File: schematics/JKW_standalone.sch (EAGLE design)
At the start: 217 parts, among them IC1 4093D, IC2 AT-MEGA-8L, IC4 ATMEGA2560-16AU, Q1 BSS84, Q10 BSS84, Q11 BSS84, Q2 BSS84, Q3 BSS84, Q4 BSS84, Q5 BSS84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

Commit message: ATm8 update: increased number of waiting steps to start 'go_back'
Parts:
- added PE: 100nF, RCLDT:C0805
- R_REED_DOWN: value 5k / n.b. (Reed) -> 5k / n.b. (Reed / 5V Honda Signal)
- R_REED_UP: value n.b. / 5k (Reed) -> n.b.(Honda Signal) / 5k (Reed)
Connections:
- net GND: now also PE.1
- net VDD: now also PE.2
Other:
- moved on the sheet: 12V_F1, 3.3V_SUPPLY, 5V_F, 5V_SUPPLY, C11, C18, C39, CP1, CP2, CP3, CP4, D12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

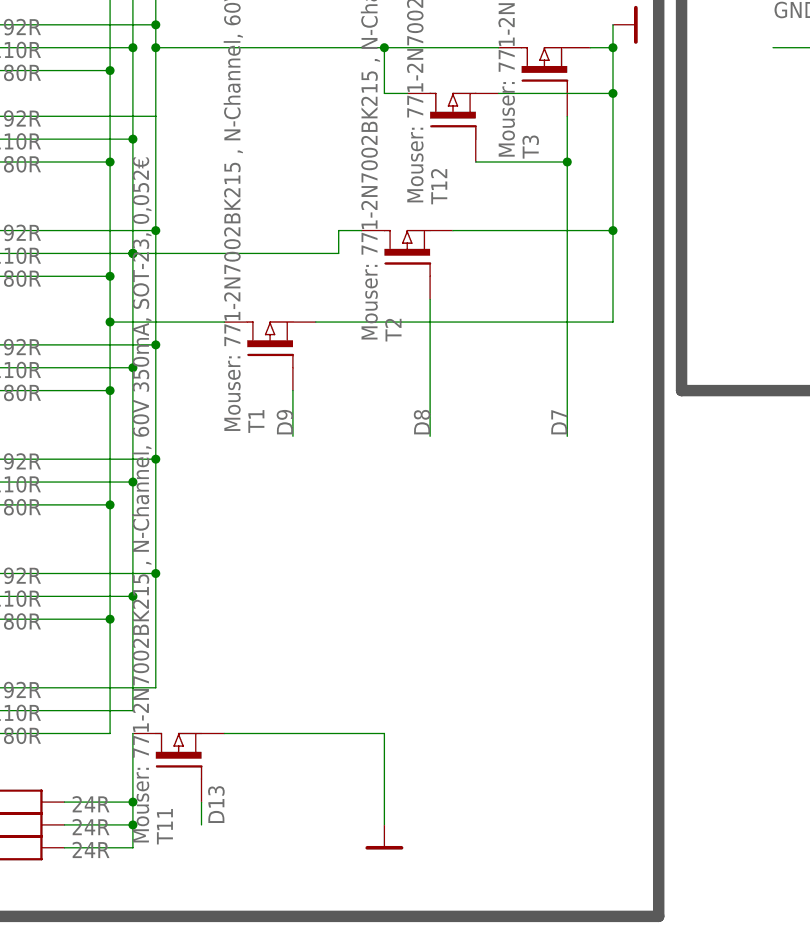
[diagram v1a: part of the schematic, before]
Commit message: added pull down for dimm transistors
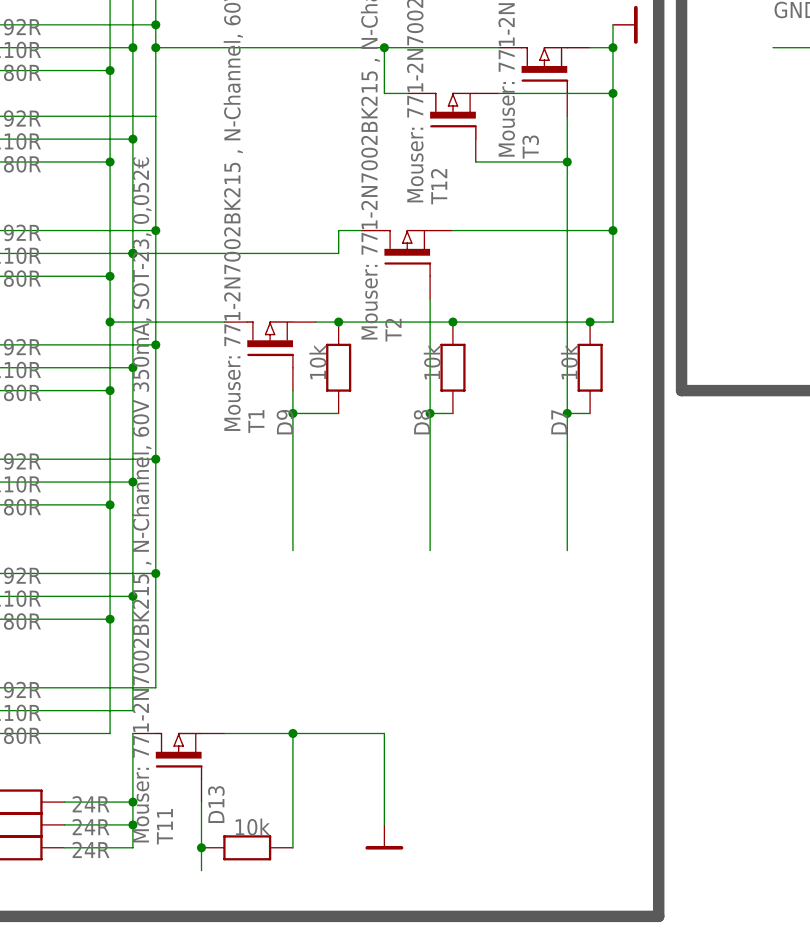
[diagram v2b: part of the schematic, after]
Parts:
- added R_B_LED_12, R_B_LED_13, R_B_LED_14, R_B_LED_15: 10k, RCLDT:R0805
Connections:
- net D13: now also R_B_LED_12.1
- net D7: now also R_B_LED_15.1
- net D8: now also R_B_LED_14.1
- net D9: now also R_B_LED_13.1
- net GND: now also R_B_LED_12.2, R_B_LED_13.2, R_B_LED_14.2, R_B_LED_15.2
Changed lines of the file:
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@@
 <?xml version="1.0" encoding="utf-8"?>
 <!DOCTYPE eagle SYSTEM "eagle.dtd">
-<eagle version="6.2">
+<eagle version="6.1">
 <drawing>
 <settings>
@@
 <part name="U$20" library="SUPPLY" deviceset="GND" device=""/>
 <part name="PE" library="RCLDT" deviceset="C" device="0805" value="100nF"/>
+<part name="R_B_LED_12" library="RCLDT" deviceset="R" device="0805" value="10k"/>
+<part name="R_B_LED_13" library="RCLDT" deviceset="R" device="0805" value="10k"/>
+<part name="R_B_LED_14" library="RCLDT" deviceset="R" device="0805" value="10k"/>
+<part name="R_B_LED_15" library="RCLDT" deviceset="R" device="0805" value="10k"/>
 </parts>
 <sheets>
@@
 <attribute name="VALUE" x="-93.98" y="2.54" size="1.778" layer="96" rot="R270"/>
 </instance>
+<instance part="R_B_LED_12" gate="G$1" x="68.58" y="-81.28" smashed="yes">
+<attribute name="VALUE" x="71.12" y="-78.105" size="1.778" layer="96" rot="R180"/>
+</instance>
+<instance part="R_B_LED_13" gate="G$1" x="78.74" y="-27.94" smashed="yes" rot="R90">
+<attribute name="VALUE" x="75.565" y="-25.4" size="1.778" layer="96" rot="R270"/>
+</instance>
+<instance part="R_B_LED_14" gate="G$1" x="91.44" y="-27.94" smashed="yes" rot="R90">
+<attribute name="VALUE" x="88.265" y="-25.4" size="1.778" layer="96" rot="R270"/>
+</instance>
+<instance part="R_B_LED_15" gate="G$1" x="106.68" y="-27.94" smashed="yes" rot="R90">
+<attribute name="VALUE" x="103.505" y="-25.4" size="1.778" layer="96" rot="R270"/>
+</instance>
 </instances>
 <busses>
@@
 <wire x1="109.22" y1="-12.7" x2="91.44" y2="-12.7" width="0.1524" layer="91"/>
 <wire x1="109.22" y1="-12.7" x2="109.22" y2="-22.86" width="0.1524" layer="91"/>
-<wire x1="109.22" y1="-22.86" x2="76.2" y2="-22.86" width="0.1524" layer="91"/>
+<wire x1="109.22" y1="-22.86" x2="106.68" y2="-22.86" width="0.1524" layer="91"/>
 <junction x="109.22" y="-12.7"/>
 <junction x="109.22" y="7.62"/>
@@
 <pinref part="T1" gate="G$1" pin="S"/>
 <pinref part="T12" gate="G$1" pin="S"/>
+<wire x1="106.68" y1="-22.86" x2="91.44" y2="-22.86" width="0.1524" layer="91"/>
+<wire x1="91.44" y1="-22.86" x2="78.74" y2="-22.86" width="0.1524" layer="91"/>
+<wire x1="78.74" y1="-22.86" x2="76.2" y2="-22.86" width="0.1524" layer="91"/>
 <wire x1="96.52" y1="2.54" x2="109.22" y2="2.54" width="0.1524" layer="91"/>
 <junction x="109.22" y="2.54"/>
+<pinref part="R_B_LED_13" gate="G$1" pin="2"/>
+<junction x="78.74" y="-22.86"/>
+<pinref part="R_B_LED_14" gate="G$1" pin="2"/>
+<junction x="91.44" y="-22.86"/>
+<pinref part="R_B_LED_15" gate="G$1" pin="2"/>
+<junction x="106.68" y="-22.86"/>
 </segment>
 <segment>
@@
 <pinref part="T11" gate="G$1" pin="S"/>
 <pinref part="U$17" gate="G$1" pin="GND"/>
-<wire x1="66.04" y1="-68.58" x2="83.82" y2="-68.58" width="0.1524" layer="91"/>
+<wire x1="66.04" y1="-68.58" x2="73.66" y2="-68.58" width="0.1524" layer="91"/>
+<wire x1="73.66" y1="-68.58" x2="83.82" y2="-68.58" width="0.1524" layer="91"/>
 <wire x1="83.82" y1="-68.58" x2="83.82" y2="-78.74" width="0.1524" layer="91"/>
+<pinref part="R_B_LED_12" gate="G$1" pin="2"/>
+<wire x1="73.66" y1="-81.28" x2="73.66" y2="-68.58" width="0.1524" layer="91"/>
+<junction x="73.66" y="-68.58"/>
 </segment>
 <segment>
@@
 <pinref part="T3" gate="G$1" pin="G"/>
 <pinref part="T12" gate="G$1" pin="G"/>
-<wire x1="104.14" y1="-5.08" x2="104.14" y2="-35.56" width="0.1524" layer="91"/>
+<wire x1="104.14" y1="-5.08" x2="104.14" y2="-33.02" width="0.1524" layer="91"/>
+<wire x1="104.14" y1="-33.02" x2="104.14" y2="-48.26" width="0.1524" layer="91"/>
 <wire x1="93.98" y1="-5.08" x2="104.14" y2="-5.08" width="0.1524" layer="91"/>
 <junction x="104.14" y="-5.08"/>
+<pinref part="R_B_LED_15" gate="G$1" pin="1"/>
+<wire x1="106.68" y1="-33.02" x2="104.14" y2="-33.02" width="0.1524" layer="91"/>
+<junction x="104.14" y="-33.02"/>
 </segment>
 </net>
@@
 </segment>
 <segment>
-<wire x1="88.9" y1="-20.32" x2="88.9" y2="-35.56" width="0.1524" layer="91"/>
+<wire x1="88.9" y1="-20.32" x2="88.9" y2="-33.02" width="0.1524" layer="91"/>
 <label x="88.9" y="-35.56" size="1.778" layer="95" rot="R90"/>
 <pinref part="T2" gate="G$1" pin="G"/>
+<pinref part="R_B_LED_14" gate="G$1" pin="1"/>
+<wire x1="88.9" y1="-33.02" x2="88.9" y2="-48.26" width="0.1524" layer="91"/>
+<wire x1="91.44" y1="-33.02" x2="88.9" y2="-33.02" width="0.1524" layer="91"/>
+<junction x="88.9" y="-33.02"/>
 </segment>
 </net>
@@
 </segment>
 <segment>
-<wire x1="73.66" y1="-30.48" x2="73.66" y2="-35.56" width="0.1524" layer="91"/>
+<wire x1="73.66" y1="-30.48" x2="73.66" y2="-33.02" width="0.1524" layer="91"/>
 <label x="73.66" y="-35.56" size="1.778" layer="95" rot="R90"/>
 <pinref part="T1" gate="G$1" pin="G"/>
+<pinref part="R_B_LED_13" gate="G$1" pin="1"/>
+<wire x1="73.66" y1="-33.02" x2="73.66" y2="-48.26" width="0.1524" layer="91"/>
+<wire x1="78.74" y1="-33.02" x2="73.66" y2="-33.02" width="0.1524" layer="91"/>
+<junction x="73.66" y="-33.02"/>
 </segment>
 </net>
@@
 <segment>
 <pinref part="T11" gate="G$1" pin="G"/>
-<wire x1="63.5" y1="-76.2" x2="63.5" y2="-78.74" width="0.1524" layer="91"/>
+<wire x1="63.5" y1="-76.2" x2="63.5" y2="-81.28" width="0.1524" layer="91"/>
 <label x="66.04" y="-78.74" size="1.778" layer="95" rot="R90"/>
-</segment>
-</net>
+<pinref part="R_B_LED_12" gate="G$1" pin="1"/>
+<wire x1="63.5" y1="-81.28" x2="63.5" y2="-83.82" width="0.1524" layer="91"/>
+<junction x="63.5" y="-81.28"/>
+</segment>
+</net>

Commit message: improved overvoltage schematic
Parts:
- removed D12: 20V-Zdiode, diode:ZENER-DIODESOD80C
- added D11: 20V-Zdiode, diode:ZENER-DIODESOT23
- added R_HB5: 600R, RCLDT:R0805
- added R_OIL_OV, R_OIL_OV1: 1k, RCLDT:R0805
- added R_R_LED_12: 220R, RCLDT:R0805
- C35: value 22p -> 100nF
- C5, C7: value 100nF -> 22pF
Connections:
- new net N$109: D11.A, R_R_LED_12.2
- new net N$110: R_HB5.1, SPEEDOSTECKER.NEUTRAL_GEAR
- new net N$111: R_OIL_OV1.1, R_WATER_UP.2, SPEEDOSTECKER.WATER_TEMP
- new net N999: R_OIL_OV.1, R_OIL_UP.1, SPEEDOSTECKER.OIL_TEMP
- net A0: now also R_OIL_OV1.2; no longer R_WATER_UP.2, SPEEDOSTECKER.WATER_TEMP
- net A1: now also R_OIL_OV.2; no longer R_OIL_UP.1, SPEEDOSTECKER.OIL_TEMP
- net GND: now also R_R_LED_12.1; no longer D12.A
- net N$1: now also D11.C; no longer D12.C
- net NG_IN: now also R_HB5.2; no longer SPEEDOSTECKER.NEUTRAL_GEAR
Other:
- moved on the sheet: D10, D18, D20, D22, D3, D_P_EX_D2, R_E2_0, R_E2_2, R_HB1, R_OIL_UP, R_WATER_UP

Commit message: Added correct overvoltage z-diode
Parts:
- removed R_B_LED_0, R_G_LED_0: 24R, RCLDT:R0805
- removed U$1: CLP6B-WKW-CD0E0233, Kolja:CLP6B-WKW-CD0E0233
- added U$22: CLM4B-RKW-CWAXBAA3, Kolja:CLM4B-RKW-CWAXBAA3
- R_R_LED_0: value 24R -> 52R
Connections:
- removed net N$63: R_G_LED_0.1, U$1.P$1
- removed net N$65: R_B_LED_0.1, U$1.P$2
- net N$16: now also U$22.CATHODE; no longer U$1.CATHODE
- net N$71: no longer R_B_LED_0.2, R_G_LED_0.2
- net VDD: now also U$22.ANODE; no longer U$1.ANODE
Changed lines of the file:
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@@
 <?xml version="1.0" encoding="utf-8"?>
 <!DOCTYPE eagle SYSTEM "eagle.dtd">
-<eagle version="6.2">
+<eagle version="6.1">
 <drawing>
 <settings>
@@
 <part name="R_G_LED_1" library="RCLDT" deviceset="R" device="0805" value="110R"/>
 <part name="R_B_LED_1" library="RCLDT" deviceset="R" device="0805" value="80R"/>
-<part name="R_R_LED_0" library="RCLDT" deviceset="R" device="0805" value="24R"/>
-<part name="R_G_LED_0" library="RCLDT" deviceset="R" device="0805" value="24R"/>
-<part name="R_B_LED_0" library="RCLDT" deviceset="R" device="0805" value="24R"/>
+<part name="R_R_LED_0" library="RCLDT" deviceset="R" device="0805" value="52R"/>
 <part name="T1" library="RCLDT" deviceset="T-P-FET" device="BSS139" value="Mouser: 771-2N7002BK215 , N-Channel, 60V 350mA, SOT-23, 0,052€"/>
 <part name="T2" library="RCLDT" deviceset="T-P-FET" device="BSS139" value="Mouser: 771-2N7002BK215 , N-Channel, 60V 350mA, SOT-23, 0,052€"/>
@@
 <part name="R_SD_PWR_UP" library="RCLDT" deviceset="R" device="0805" value="10k"/>
 <part name="R_RES_UP" library="RCLDT" deviceset="R" device="0805" value="10k"/>
-<part name="U$1" library="Kolja" deviceset="CLP6B-WKW-CD0E0233" device=""/>
 <part name="U$3" library="Kolja" deviceset="CLM4B-BKW-CTBVA363" device=""/>
 <part name="U$11" library="Kolja" deviceset="CLM4B-RKW-CWAXBAA3" device=""/>
@@
 <part name="R_HB5" library="RCLDT" deviceset="R" device="0805" value="600R"/>
 <part name="R_OIL_OV1" library="RCLDT" deviceset="R" device="0805" value="1k"/>
+<part name="U$22" library="Kolja" deviceset="CLM4B-RKW-CWAXBAA3" device=""/>
 </parts>
 <sheets>
@@
 <attribute name="VALUE" x="53.34" y="-75.565" size="1.778" layer="96" rot="R180"/>
 </instance>
-<instance part="R_G_LED_0" gate="G$1" x="43.18" y="-78.74" smashed="yes">
-<attribute name="VALUE" x="53.34" y="-78.105" size="1.778" layer="96" rot="R180"/>
-</instance>
-<instance part="R_B_LED_0" gate="G$1" x="43.18" y="-81.28" smashed="yes">
-<attribute name="VALUE" x="53.34" y="-80.645" size="1.778" layer="96" rot="R180"/>
-</instance>
 <instance part="T1" gate="G$1" x="71.12" y="-25.4" rot="MR90"/>
 <instance part="T2" gate="G$1" x="86.36" y="-15.24" rot="MR90"/>
@@
 <instance part="R_SD_PWR_UP" gate="G$1" x="-35.56" y="119.38" rot="MR90"/>
 <instance part="R_RES_UP" gate="G$1" x="-294.64" y="208.28" rot="MR90"/>
-<instance part="U$1" gate="G$1" x="15.24" y="-76.2"/>
 <instance part="U$3" gate="G$1" x="383.54" y="2.54" rot="R90"/>
 <instance part="U$11" gate="G$1" x="370.84" y="2.54" rot="R90"/>
@@
 <instance part="R_HB5" gate="G$1" x="91.44" y="187.96" rot="R180"/>
 <instance part="R_OIL_OV1" gate="G$1" x="58.42" y="139.7" rot="R180"/>
+<instance part="U$22" gate="G$1" x="25.4" y="-76.2"/>
 </instances>
 <busses>
@@
 <segment>
 <pinref part="SUPPLY15" gate="G$1" pin="VDD"/>
-<wire x1="7.62" y1="-76.2" x2="-2.54" y2="-76.2" width="0.1524" layer="91"/>
-<pinref part="U$1" gate="G$1" pin="ANODE"/>
+<wire x1="20.32" y1="-76.2" x2="-2.54" y2="-76.2" width="0.1524" layer="91"/>
+<pinref part="U$22" gate="G$1" pin="ANODE"/>
 </segment>
 <segment>
@@
 <pinref part="T11" gate="G$1" pin="G"/>
 <wire x1="63.5" y1="-76.2" x2="63.5" y2="-81.28" width="0.1524" layer="91"/>
-<label x="66.04" y="-78.74" size="1.778" layer="95" rot="R90"/>
 <pinref part="R_B_LED_12" gate="G$1" pin="1"/>
 <wire x1="63.5" y1="-81.28" x2="63.5" y2="-83.82" width="0.1524" layer="91"/>
 <junction x="63.5" y="-81.28"/>
+<label x="60.96" y="-86.36" size="1.778" layer="95"/>
 </segment>
 </net>
@@
 </segment>
 </net>
-<net name="N$65" class="0">
-<segment>
-<wire x1="38.1" y1="-81.28" x2="20.32" y2="-81.28" width="0.1524" layer="91"/>
-<pinref part="R_B_LED_0" gate="G$1" pin="1"/>
-<pinref part="U$1" gate="G$1" pin="P$2"/>
-</segment>
-</net>
 <net name="N$24" class="0">
 <segment>
@@
 <net name="N$71" class="0">
 <segment>
-<pinref part="R_B_LED_0" gate="G$1" pin="2"/>
 <pinref part="T11" gate="G$1" pin="D"/>
-<wire x1="48.26" y1="-81.28" x2="55.88" y2="-81.28" width="0.1524" layer="91"/>
-<wire x1="55.88" y1="-81.28" x2="55.88" y2="-78.74" width="0.1524" layer="91"/>
-<pinref part="R_G_LED_0" gate="G$1" pin="2"/>
-<wire x1="55.88" y1="-78.74" x2="55.88" y2="-76.2" width="0.1524" layer="91"/>
 <wire x1="55.88" y1="-76.2" x2="55.88" y2="-68.58" width="0.1524" layer="91"/>
-<wire x1="48.26" y1="-78.74" x2="55.88" y2="-78.74" width="0.1524" layer="91"/>
 <pinref part="R_R_LED_0" gate="G$1" pin="2"/>
 <wire x1="48.26" y1="-76.2" x2="55.88" y2="-76.2" width="0.1524" layer="91"/>
-<junction x="55.88" y="-78.74"/>
-<junction x="55.88" y="-76.2"/>
-</segment>
-</net>
-<net name="N$16" class="0">
-<segment>
-<pinref part="R_R_LED_0" gate="G$1" pin="1"/>
-<pinref part="U$1" gate="G$1" pin="CATHODE"/>
-<wire x1="20.32" y1="-76.2" x2="38.1" y2="-76.2" width="0.1524" layer="91"/>
-</segment>
-</net>
-<net name="N$63" class="0">
-<segment>
-<wire x1="20.32" y1="-78.74" x2="38.1" y2="-78.74" width="0.1524" layer="91"/>
-<pinref part="R_G_LED_0" gate="G$1" pin="1"/>
-<pinref part="U$1" gate="G$1" pin="P$1"/>
 </segment>
 </net>
@@
 </segment>
 </net>
+<net name="N$16" class="0">
+<segment>
+<pinref part="R_R_LED_0" gate="G$1" pin="1"/>
+<wire x1="27.94" y1="-76.2" x2="28.448" y2="-76.2" width="0.1524" layer="91"/>
+<pinref part="U$22" gate="G$1" pin="CATHODE"/>
+<wire x1="28.448" y1="-76.2" x2="38.1" y2="-76.2" width="0.1524" layer="91"/>
+<junction x="28.448" y="-76.2"/>
+</segment>
+</net>

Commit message: added reset from ATM328 to 2560
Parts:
- added R_L3: 1k, RCLDT:R0805
- IC2: value AT-MEGA-8L -> AT-MEGA-328P-AU
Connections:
- net RESETAVR_AT8: now also IC4.(ICP1)PD4, R_L3.2
- net VDD: now also R_L3.1
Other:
- note added: "ATmega328P-AU"
- note removed: "ATmega8"
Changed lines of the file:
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@@
 <?xml version="1.0" encoding="utf-8"?>
 <!DOCTYPE eagle SYSTEM "eagle.dtd">
-<eagle version="6.1">
+<eagle version="6.2">
 <drawing>
 <settings>
@@
 <part name="U$161" library="SUPPLY" deviceset="GND" device=""/>
 <part name="GND4" library="SparkFun" deviceset="GND" device=""/>
-<part name="IC2" library="µP´s+Pic´s" deviceset="AT-MEGA-8" device="" value="AT-MEGA-8L"/>
+<part name="IC2" library="µP´s+Pic´s" deviceset="AT-MEGA-8" device="" value="AT-MEGA-328P-AU"/>
 <part name="AT8_REF" library="RCLDT" deviceset="R" device="0805" value="10R"/>
 <part name="U$5" library="SUPPLY" deviceset="GND" device=""/>
@@
 <part name="R_OIL_OV1" library="RCLDT" deviceset="R" device="0805" value="1k"/>
 <part name="U$22" library="Kolja" deviceset="CLM4B-RKW-CWAXBAA3" device=""/>
+<part name="R_L3" library="RCLDT" deviceset="R" device="0805" value="1k"/>
+<part name="SUPPLY22" library="supply2" deviceset="VDD" device=""/>
 </parts>
 <sheets>
@@
 <text x="-19.812" y="165.608" size="1.778" layer="91">ARD_TX</text>
 <text x="228.28" y="246.38" size="3.81" layer="95">i2c_temp</text>
-<text x="-220.98" y="66.04" size="5.08" layer="95">ATmega8</text>
+<text x="-220.98" y="66.04" size="5.08" layer="95">ATmega328P-AU</text>
 <text x="340.36" y="55.88" size="3.81" layer="95">Lichtlein &amp; Blinker</text>
 <text x="-7.62" y="53.34" size="3.81" layer="95">Instrumenten Beleuchtung</text>
@@
 <instance part="R_OIL_OV1" gate="G$1" x="58.42" y="139.7" rot="R180"/>
 <instance part="U$22" gate="G$1" x="25.4" y="-76.2"/>
+<instance part="R_L3" gate="G$1" x="-142.24" y="53.34" smashed="yes">
+<attribute name="VALUE" x="-132.08" y="53.975" size="1.778" layer="96" rot="R180"/>
+</instance>
+<instance part="SUPPLY22" gate="G$1" x="-149.86" y="60.96"/>
 </instances>
 <busses>
@@
 <junction x="-96.52" y="-5.08"/>
 </segment>
+<segment>
+<pinref part="R_L3" gate="G$1" pin="1"/>
+<pinref part="SUPPLY22" gate="G$1" pin="VDD"/>
+<wire x1="-147.32" y1="53.34" x2="-149.86" y2="53.34" width="0.1524" layer="91"/>
+<wire x1="-149.86" y1="53.34" x2="-149.86" y2="58.42" width="0.1524" layer="91"/>
+</segment>
 </net>
 <net name="CONNECT" class="0">
@@
 </segment>
 <segment>
-<wire x1="-134.62" y1="43.18" x2="-134.62" y2="71.12" width="0.1524" layer="91"/>
+<wire x1="-134.62" y1="43.18" x2="-134.62" y2="53.34" width="0.1524" layer="91"/>
 <label x="-134.3152" y="68.6816" size="1.778" layer="95" rot="R270"/>
 <pinref part="JP2" gate="A" pin="2"/>
+<pinref part="R_L3" gate="G$1" pin="2"/>
+<wire x1="-134.62" y1="53.34" x2="-134.62" y2="71.12" width="0.1524" layer="91"/>
+<wire x1="-137.16" y1="53.34" x2="-134.62" y2="53.34" width="0.1524" layer="91"/>
+<junction x="-134.62" y="53.34"/>
+</segment>
+<segment>
+<pinref part="IC4" gate="1" pin="(ICP1)PD4"/>
+<wire x1="-185.42" y1="162.56" x2="-170.18" y2="162.56" width="0.1524" layer="91"/>
+<label x="-182.88" y="162.56" size="1.778" layer="95"/>
 </segment>
 </net>

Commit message: Moved LED's to port expander
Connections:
- new net PE_A3: T9.G, U$19.A3
- new net PE_A4: T7.G, U$19.A4
- new net PE_A5: T6.G, U$19.A5
- new net PE_A6: T10.G, U$19.A6
- new net PE_A7: T8.G, U$19.A7
- net D42: no longer T7.G
- net D43: no longer T6.G
- net D44: no longer T10.G
- net D45: no longer T9.G
- net D46: no longer T8.G
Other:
- moved on the sheet: 12V_F1, 3.3V_SUPPLY, 5V_F, 5V_SUPPLY, C11, C18, C39, CP1, CP2, CP3, CP4, D11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

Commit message: changed controller
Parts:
- removed IC2: AT-MEGA-328P-AU, µP´s+Pic´s:AT-MEGA-8
- added U$1: ATMEGA328P-AU, Kolja:ATMEGA328P-AU
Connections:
- net A2: now also U$1.(PCINT20/XCK/T0)PD4; no longer IC2.T0/PD4
- net ARD_RES_OUT: now also U$1.(ADC5/PCINT13/SCL)PC5; no longer IC2.ADC5/PC5
- net CONNECT: now also U$1.(INT0/PCINT18)PD2; no longer IC2.INT0/PD2
- net D6: now also U$1.(PCINT19/OC2B/INT1)PD3; no longer IC2.INT1/PD3
- net GND: now also U$1.GND, U$1.GND@1, U$1.GND@2; no longer IC2.AGND, IC2.GND, IC2.GND@1
- net M1: now also U$1.(ADC0/PCINT8)PC0; no longer IC2.ADC0/PC0
- net M2: now also U$1.(ADC1/PCINT9)PC1; no longer IC2.ADC1/PC1
- net M3: now also U$1.(ADC2/PCINT10)PC2; no longer IC2.ADC2/PC2
- net M4: now also U$1.(ADC3/PCINT11)PC3; no longer IC2.ADC3/PC3
- net MISO_AT8: now also U$1.(PCINT4/MISO)PB4; no longer IC2.MISO/PB4
- net MOSI_AT8: now also U$1.(PCINT3/OC2A/MOSI)PB3; no longer IC2.MOSI/PB3
- net N$14: now also U$1.(PCINT23/AIN1)PD7; no longer IC2.AIN1/PD7
- net N$18: now also U$1.(PCINT22/OC0A/AIN0)PD6; no longer IC2.AIN0/PD6
- net N$20: now also U$1.(PCINT21/OC0B/T1)PD5; no longer IC2.T1/PD5
- net N$3: now also U$1.AREF, U$1.AVCC; no longer IC2.AREF, IC2.AVCC
- net RESETAVR_AT8: no longer IC2.RESET
- net RX3: now also U$1.(TXD/PCINT17)PD1; no longer IC2.TXD/PD1
- net SCK_AT8: now also U$1.(PCINT5/SCK)PB5; no longer IC2.SCK/PB5
- net TX3: now also U$1.(RXD/PCINT16)PD0; no longer IC2.RXD/PD0
- net V_AT8_BUFFERED: now also U$1.VCC@1, U$1.VCC@2; no longer IC2.VDD, IC2.VDD@1
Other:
- moved on the sheet: AT8_REF, C1, C2, C3, C_EMERGENCY, D9

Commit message: Moved AT in place
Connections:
- net RESETAVR_AT8: now also U$1.(!RESET!/PCINT14)PC6
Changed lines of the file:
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@@
 <?xml version="1.0" encoding="utf-8"?>
 <!DOCTYPE eagle SYSTEM "eagle.dtd">
-<eagle version="6.2">
+<eagle version="6.1">
 <drawing>
 <settings>
@@
 <wire x1="-241.3" y1="-35.56" x2="-226.06" y2="-35.56" width="0.1524" layer="91"/>
 <label x="-246.38" y="-35.56" size="1.778" layer="95"/>
+<pinref part="U$1" gate="G$1" pin="(!RESET!/PCINT14)PC6"/>
 </segment>
 <segment>
